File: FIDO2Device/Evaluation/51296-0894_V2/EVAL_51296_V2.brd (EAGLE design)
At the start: 25 x 38 mm, 25 parts, among them CN1 51296-0894, CN2 IF_6PIN, CN3 IF_3PIN, CN4 IF_4PIN, Q1 BSS84AKQBZ, U1 RV-3028-C7

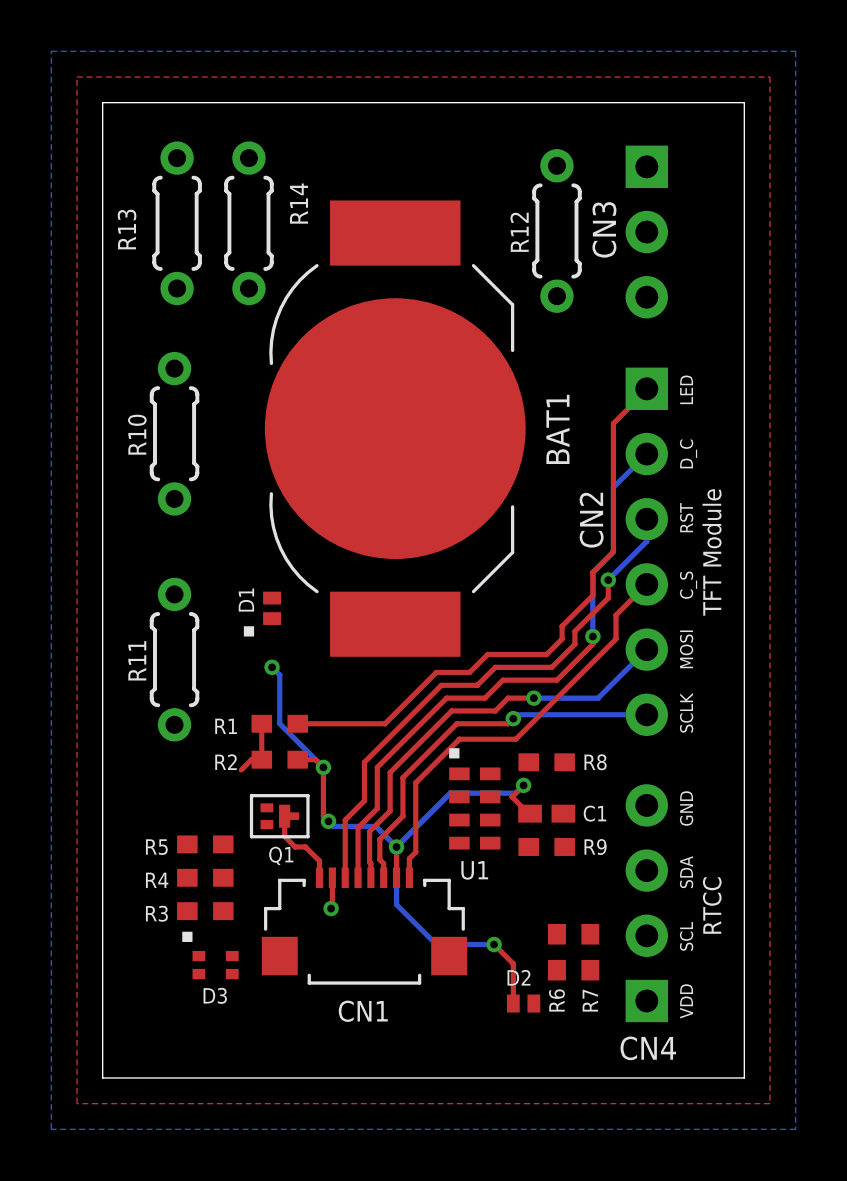
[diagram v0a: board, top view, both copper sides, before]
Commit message: レイアウトを修正
・電源周りを配線
・シルクを追加（LED配線用の注記）
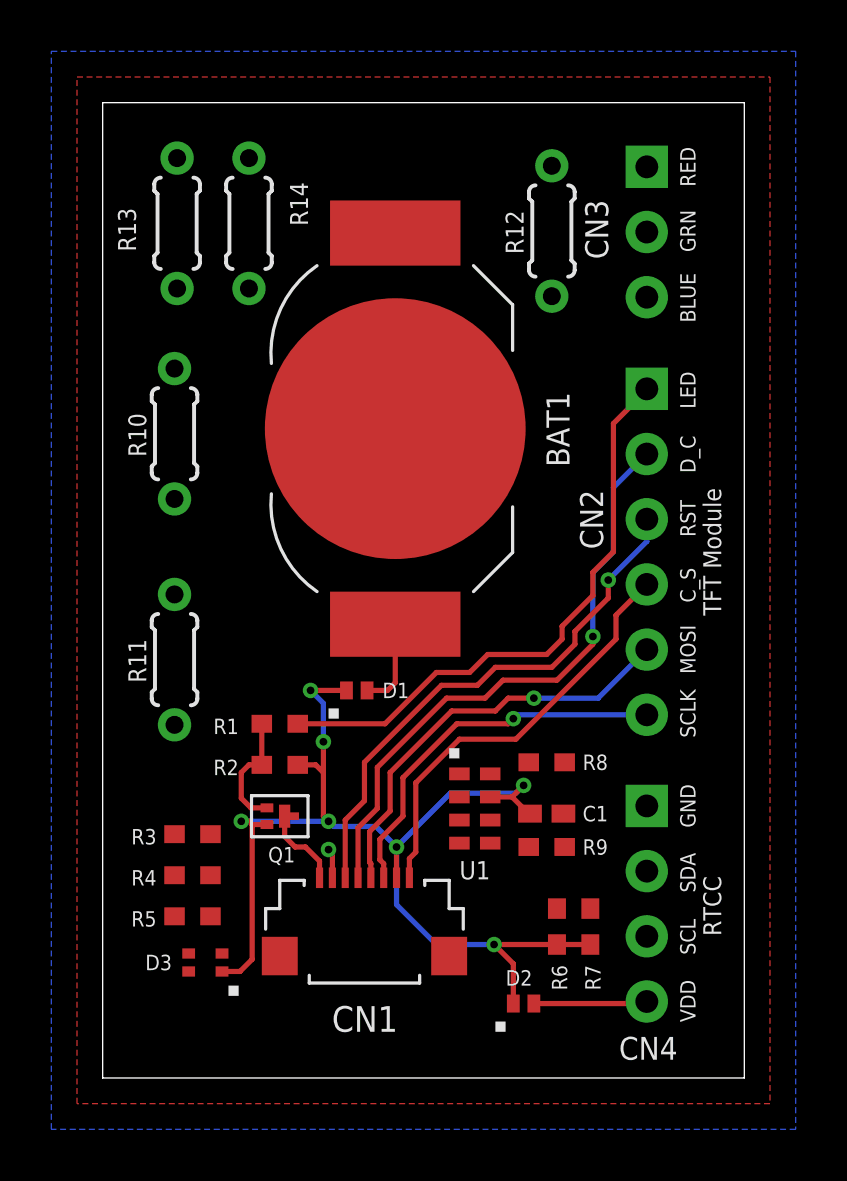
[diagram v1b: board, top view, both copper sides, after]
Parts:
- moved CN4 7.60 mm to (21.2, 10.6), turned to 270 degrees
- moved D1 4.60 mm to (9.90, 15.1), turned to 0 degrees
- moved R3 3.04 mm to (3.50, 9.50)
- moved R5 2.84 mm to (3.50, 6.30)
- moved R6 1.00 mm to (17.7, 5.90)
- moved R7 1.00 mm to (19.0, 5.90)
- moved R4 0.51 mm to (3.50, 7.90)
- moved D3 0.41 mm to (4.00, 4.50), turned to 180 degrees
- moved R2 0.20 mm to (6.90, 12.2)
- moved R12 0.20 mm to (17.5, 33.0)
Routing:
- net VDD: track 29.3 -> 44.7 mm, vias 6 -> 7
- net VDD_NRF: track 0.03 -> 4.46 mm
- net N$2: track 0.00 -> 3.50 mm
- net N$1: track 2.37 -> 4.68 mm
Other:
- board text added: "BLUE"
- board text added: "GRN"
- board text added: "RED"

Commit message: レイアウトを修正
・RTCC周りを配線
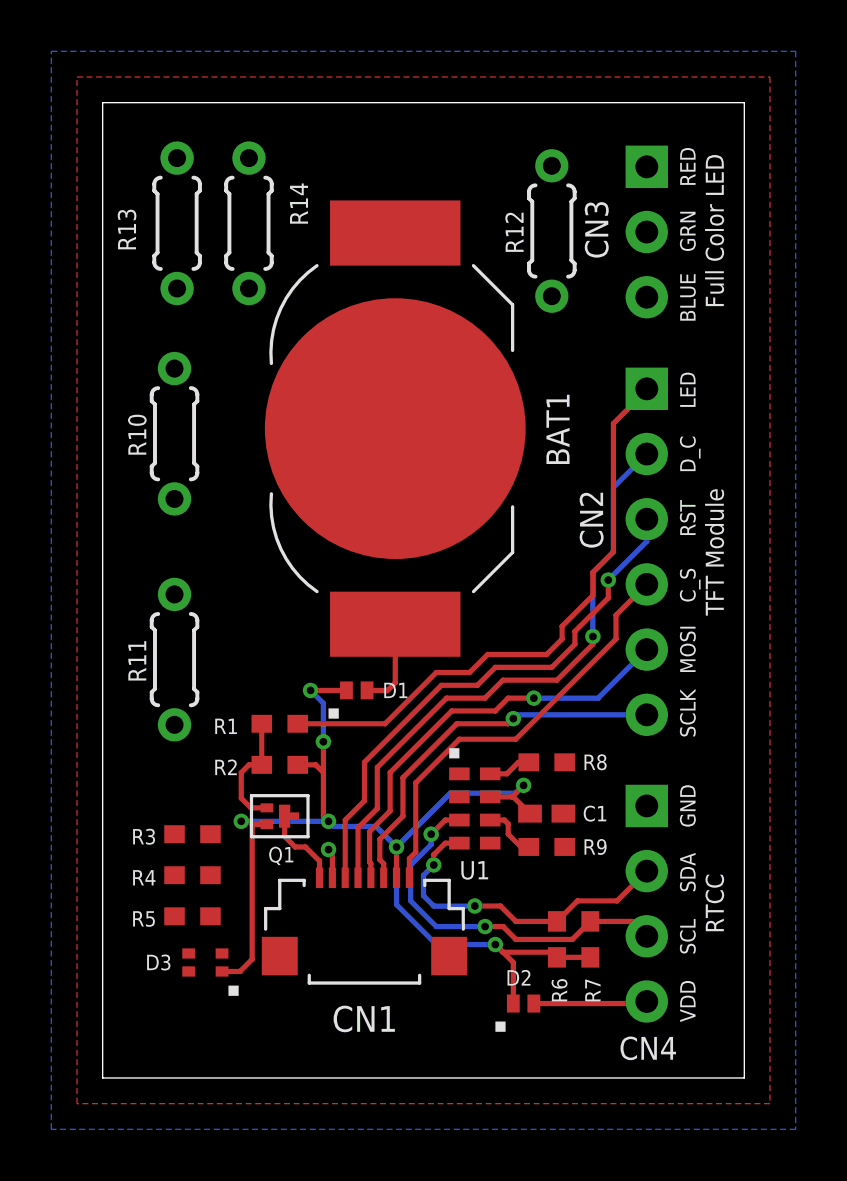
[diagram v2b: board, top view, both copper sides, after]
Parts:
- moved R6 0.50 mm to (17.7, 5.40)
- moved R7 0.50 mm to (19.0, 5.40)
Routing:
- net TWI_SCL: track 0.00 -> 14.6 mm, vias 0 -> 2
- net TWI_SDA: track 0.00 -> 12.9 mm, vias 0 -> 2
- net N$3: track 0.00 -> 2.17 mm
- net N$4: track 0.00 -> 1.69 mm
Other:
- board text added: "Full Color LED"
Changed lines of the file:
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@@
 <layer number="49" name="Reference" color="7" fill="1" visible="no" active="yes"/>
 <layer number="50" name="dxf" color="7" fill="1" visible="no" active="no"/>
-<layer number="51" name="tDocu" color="7" fill="1" visible="no" active="yes"/>
-<layer number="52" name="bDocu" color="7" fill="1" visible="no" active="yes"/>
+<layer number="51" name="tDocu" color="7" fill="1" visible="yes" active="yes"/>
+<layer number="52" name="bDocu" color="7" fill="1" visible="yes" active="yes"/>
 <layer number="53" name="tGND_GNDA" color="7" fill="9" visible="no" active="no"/>
 <layer number="54" name="bGND_GNDA" color="1" fill="9" visible="no" active="no"/>
@@
 <text x="22.5" y="24.3" size="0.6" layer="21" rot="R90" align="top-center">D_C</text>
 <text x="22.5" y="26.8" size="0.6" layer="21" rot="R90" align="top-center">LED</text>
-<text x="23.4" y="20.5" size="0.7" layer="21" rot="R90" align="top-center">TFT Module</text>
-<text x="23.4" y="6.7" size="0.7" layer="21" rot="R90" align="top-center">RTCC</text>
+<text x="23.5" y="20.5" size="0.7" layer="21" rot="R90" align="top-center">TFT Module</text>
+<text x="23.5" y="6.8" size="0.7" layer="21" rot="R90" align="top-center">RTCC</text>
 <rectangle x1="8.8" y1="14" x2="9.2" y2="14.4" layer="21"/>
 <rectangle x1="15.3" y1="1.8" x2="15.7" y2="2.2" layer="21"/>
@@
 <text x="22.5" y="33" size="0.6" layer="21" rot="R90" align="top-center">GRN</text>
 <text x="22.5" y="35.5" size="0.6" layer="21" rot="R90" align="top-center">RED</text>
+<text x="23.5" y="33" size="0.7" layer="21" rot="R90" align="top-center">Full Color LED</text>
 </plain>
 <attributes>
@@
 <attribute name="VALUE" x="12.4" y="12.15" size="0.7112" layer="27" rot="R270"/>
 </element>
-<element name="R6" library="Parts" package="R0402N" value="10k" x="17.7" y="5.9" smashed="yes" rot="R270">
-<attribute name="NAME" x="17.5" y="4.4" size="0.6" layer="25" rot="R270"/>
-<attribute name="VALUE" x="16.4" y="6.4" size="0.6" layer="27" rot="R270"/>
-</element>
-<element name="R7" library="Parts" package="R0402N" value="10k" x="19" y="5.9" smashed="yes" rot="R270">
-<attribute name="NAME" x="18.8" y="4.4" size="0.6" layer="25" rot="R270"/>
-<attribute name="VALUE" x="17.7" y="6.4" size="0.6" layer="27" rot="R270"/>
+<element name="R6" library="Parts" package="R0402N" value="10k" x="17.7" y="5.4" smashed="yes" rot="R270">
+<attribute name="NAME" x="17.5" y="3.9" size="0.6" layer="25" rot="R270"/>
+<attribute name="VALUE" x="16.4" y="5.9" size="0.6" layer="27" rot="R270"/>
+</element>
+<element name="R7" library="Parts" package="R0402N" value="10k" x="19" y="5.4" smashed="yes" rot="R270">
+<attribute name="NAME" x="18.8" y="3.9" size="0.6" layer="25" rot="R270"/>
+<attribute name="VALUE" x="17.7" y="5.9" size="0.6" layer="27" rot="R270"/>
 </element>
 <element name="R8" library="Parts" package="R0402N" value="10k" x="17.3" y="12.3" smashed="yes" rot="R180">
@@
 <via x="11.45" y="9" extent="1-16" drill="0.3"/>
 <via x="8.1" y="15.1" extent="1-16" drill="0.3"/>
-<via x="15.25" y="5.2" extent="1-16" drill="0.3"/>
+<via x="15.3" y="5.2" extent="1-16" drill="0.3"/>
 <via x="8.8" y="10" extent="1-16" drill="0.3"/>
 <wire x1="9" y1="9.8" x2="10.65" y2="9.8" width="0.2032" layer="16"/>
 <wire x1="11.45" y1="9" x2="10.65" y2="9.8" width="0.2032" layer="16"/>
 <wire x1="11.45" y1="7.8" x2="11.45" y2="9" width="0.2032" layer="1"/>
-<wire x1="15.25" y1="5.2" x2="13" y2="5.2" width="0.2032" layer="16"/>
+<wire x1="15.3" y1="5.2" x2="13" y2="5.2" width="0.2032" layer="16"/>
 <wire x1="13" y1="5.2" x2="11.45" y2="6.75" width="0.2032" layer="16"/>
 <wire x1="11.45" y1="9" x2="11.45" y2="6.75" width="0.2032" layer="16"/>
@@
 <wire x1="5.825" y1="4.625" x2="5.35" y2="4.15" width="0.2032" layer="1"/>
 <wire x1="4.65" y1="4.15" x2="5.35" y2="4.15" width="0.2032" layer="1"/>
-<wire x1="17.7" y1="5.2" x2="15.25" y2="5.2" width="0.2032" layer="1"/>
-<wire x1="16" y1="2.9" x2="16" y2="4.45" width="0.2032" layer="1"/>
-<wire x1="16" y1="4.45" x2="15.25" y2="5.2" width="0.2032" layer="1"/>
-<wire x1="17.7" y1="5.2" x2="19" y2="5.2" width="0.2032" layer="1"/>
 <wire x1="15.95" y1="10.95" x2="15.1" y2="10.95" width="0.2032" layer="1"/>
-<wire x1="16.6" y1="10.3" x2="15.95" y2="10.95" width="0.2032" layer="1"/>
 <wire x1="8.1" y1="15.1" x2="8.6" y2="14.6" width="0.2032" layer="16"/>
 <wire x1="8.6" y1="14.6" x2="8.6" y2="13.1" width="0.2032" layer="16"/>
@@
 <wire x1="7.6" y1="12.2" x2="8.3" y2="12.2" width="0.2032" layer="1"/>
 <wire x1="8.3" y1="12.2" x2="8.6" y2="11.9" width="0.2032" layer="1"/>
-<wire x1="16.6" y1="10.3" x2="16.65" y2="10.3" width="0" layer="19" extent="1-1"/>
-<wire x1="2.8" y1="13.76" x2="5.4" y2="10" width="0" layer="19" extent="16-16"/>
+<wire x1="16" y1="2.9" x2="16" y2="4.5" width="0.2032" layer="1"/>
+<wire x1="16" y1="4.5" x2="15.3" y2="5.2" width="0.2032" layer="1"/>
+<wire x1="19" y1="4.7" x2="17.7" y2="4.7" width="0.2032" layer="1"/>
+<wire x1="17.7" y1="4.7" x2="17.5" y2="4.9" width="0.2032" layer="1"/>
+<wire x1="17.5" y1="4.9" x2="15.6" y2="4.9" width="0.2032" layer="1"/>
+<wire x1="15.6" y1="4.9" x2="15.3" y2="5.2" width="0.2032" layer="1"/>
+<wire x1="15.95" y1="10.95" x2="16" y2="10.95" width="0.2032" layer="1"/>
+<wire x1="16" y1="10.95" x2="16.65" y2="10.3" width="0.2032" layer="1"/>
+<wire x1="5.4" y1="10" x2="2.8" y2="13.76" width="0" layer="19" extent="16-16"/>
 </signal>
 <signal name="LED_CTRL">
@@
 <contactref element="U1" pad="4"/>
 <contactref element="R6" pad="1"/>
-<wire x1="17.7" y1="6.6" x2="21.2" y2="8.06" width="0" layer="19" extent="1-1"/>
-<wire x1="13.9" y1="9.15" x2="17.7" y2="6.6" width="0" layer="19" extent="1-1"/>
+<via x="14.5" y="6.7" extent="1-16" drill="0.3"/>
+<via x="12.9" y="8.3" extent="1-16" drill="0.3"/>
+<wire x1="14.5" y1="6.7" x2="12.9" y2="6.7" width="0.2032" layer="16"/>
+<wire x1="12.9" y1="6.7" x2="12.5" y2="7.1" width="0.2032" layer="16"/>
+<wire x1="12.5" y1="7.1" x2="12.5" y2="7.9" width="0.2032" layer="16"/>
+<wire x1="12.5" y1="7.9" x2="12.9" y2="8.3" width="0.2032" layer="16"/>
+<wire x1="13.9" y1="9.15" x2="13.35" y2="9.15" width="0.2032" layer="1"/>
+<wire x1="13.35" y1="9.15" x2="12.9" y2="8.7" width="0.2032" layer="1"/>
+<wire x1="12.9" y1="8.3" x2="12.9" y2="8.7" width="0.2032" layer="1"/>
+<wire x1="17.7" y1="6.1" x2="16.1" y2="6.1" width="0.2032" layer="1"/>
+<wire x1="16.1" y1="6.1" x2="15.5" y2="6.7" width="0.2032" layer="1"/>
+<wire x1="15.5" y1="6.7" x2="14.5" y2="6.7" width="0.2032" layer="1"/>
+<wire x1="21.2" y1="8.06" x2="20.04" y2="6.9" width="0.2032" layer="1"/>
+<wire x1="20.04" y1="6.9" x2="18.5" y2="6.9" width="0.2032" layer="1"/>
+<wire x1="17.7" y1="6.1" x2="18.5" y2="6.9" width="0.2032" layer="1"/>
 </signal>
 <signal name="TWI_SCL">
@@
 <contactref element="U1" pad="3"/>
 <contactref element="R7" pad="1"/>
-<wire x1="19" y1="6.6" x2="21.2" y2="5.52" width="0" layer="19" extent="1-1"/>
-<wire x1="13.9" y1="10.05" x2="19" y2="6.6" width="0" layer="19" extent="1-1"/>
+<via x="14.9" y="5.9" extent="1-16" drill="0.3"/>
+<via x="12.8" y="9.5" extent="1-16" drill="0.3"/>
+<wire x1="12.8" y1="9.5" x2="12.8" y2="9.1" width="0.2032" layer="16"/>
+<wire x1="12.8" y1="9.1" x2="12" y2="8.3" width="0.2032" layer="16"/>
+<wire x1="12" y1="8.3" x2="12" y2="6.9" width="0.2032" layer="16"/>
+<wire x1="12" y1="6.9" x2="13" y2="5.9" width="0.2032" layer="16"/>
+<wire x1="13" y1="5.9" x2="14.9" y2="5.9" width="0.2032" layer="16"/>
+<wire x1="13.9" y1="10.05" x2="13.35" y2="10.05" width="0.2032" layer="1"/>
+<wire x1="13.35" y1="10.05" x2="12.8" y2="9.5" width="0.2032" layer="1"/>
+<wire x1="14.9" y1="5.9" x2="15.6" y2="5.9" width="0.2032" layer="1"/>
+<wire x1="15.6" y1="5.9" x2="16.1" y2="5.4" width="0.2032" layer="1"/>
+<wire x1="16.1" y1="5.4" x2="18.3" y2="5.4" width="0.2032" layer="1"/>
+<wire x1="18.3" y1="5.4" x2="19" y2="6.1" width="0.2032" layer="1"/>
+<wire x1="19" y1="6.1" x2="20.62" y2="6.1" width="0.2032" layer="1"/>
+<wire x1="20.62" y1="6.1" x2="21.2" y2="5.52" width="0.2032" layer="1"/>
 </signal>
 <signal name="N$2">
@@
 <contactref element="U1" pad="6"/>
 <contactref element="R9" pad="2"/>
-<wire x1="15.1" y1="10.05" x2="16.6" y2="9" width="0" layer="19" extent="1-1"/>
+<wire x1="16.6" y1="9" x2="16.3" y2="9" width="0.2032" layer="1"/>
+<wire x1="16.3" y1="9" x2="15.8" y2="9.5" width="0.2032" layer="1"/>
+<wire x1="15.1" y1="10.05" x2="15.65" y2="10.05" width="0.2032" layer="1"/>
+<wire x1="15.65" y1="10.05" x2="15.8" y2="9.9" width="0.2032" layer="1"/>
+<wire x1="15.8" y1="9.9" x2="15.8" y2="9.5" width="0.2032" layer="1"/>
 </signal>
 <signal name="N$4">
 <contactref element="U1" pad="8"/>
 <contactref element="R8" pad="2"/>
-<wire x1="15.1" y1="11.85" x2="16.6" y2="12.3" width="0" layer="19" extent="1-1"/>
+<wire x1="16.6" y1="12.3" x2="16.2" y2="12.3" width="0.2032" layer="1"/>
+<wire x1="16.2" y1="12.3" x2="15.75" y2="11.85" width="0.2032" layer="1"/>
+<wire x1="15.1" y1="11.85" x2="15.75" y2="11.85" width="0.2032" layer="1"/>
 </signal>
 <signal name="LED_R">

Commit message: レイアウトを修正
・MOSFET周りの配線レイアウトを修正
・ボタン乾電池の向きを修正
（基板の最端に寄せました）
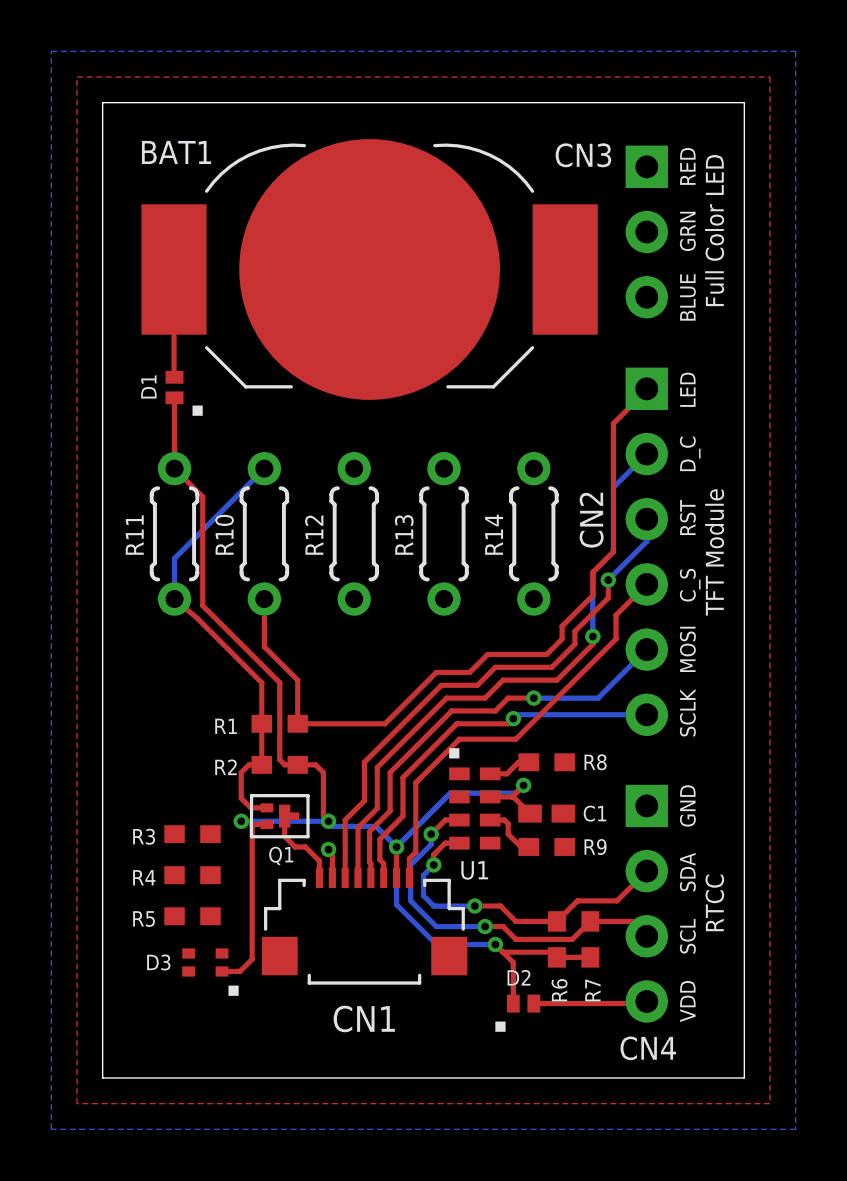
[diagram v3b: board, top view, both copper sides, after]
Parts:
- moved R14 16.4 mm to (16.8, 21.2)
- moved R13 16.0 mm to (13.3, 21.2)
- moved R12 14.1 mm to (9.80, 21.2)
- moved D1 13.8 mm to (2.80, 26.9), turned to 90 degrees
- moved BAT1 6.28 mm to (10.4, 31.5), turned to 180 degrees
- moved R10 5.24 mm to (6.30, 21.2), turned to 90 degrees
- moved R11 4.90 mm to (2.80, 21.2), turned to 90 degrees
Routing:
- net N$1: track 4.68 -> 17.5 mm
- net VDD: track 44.9 -> 56.7 mm, vias 7 -> 5
- net LED_CTRL: track 22.8 -> 28.2 mm
- net N$2: track 3.50 -> 4.21 mm
